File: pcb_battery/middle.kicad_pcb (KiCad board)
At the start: 2 copper layers, 100 x 29.9 mm, 8 parts, among them J1 BAT+, J2 BAT-, J3 TOP+, J4 BOT+, J5 TOP-, J6 BOT-

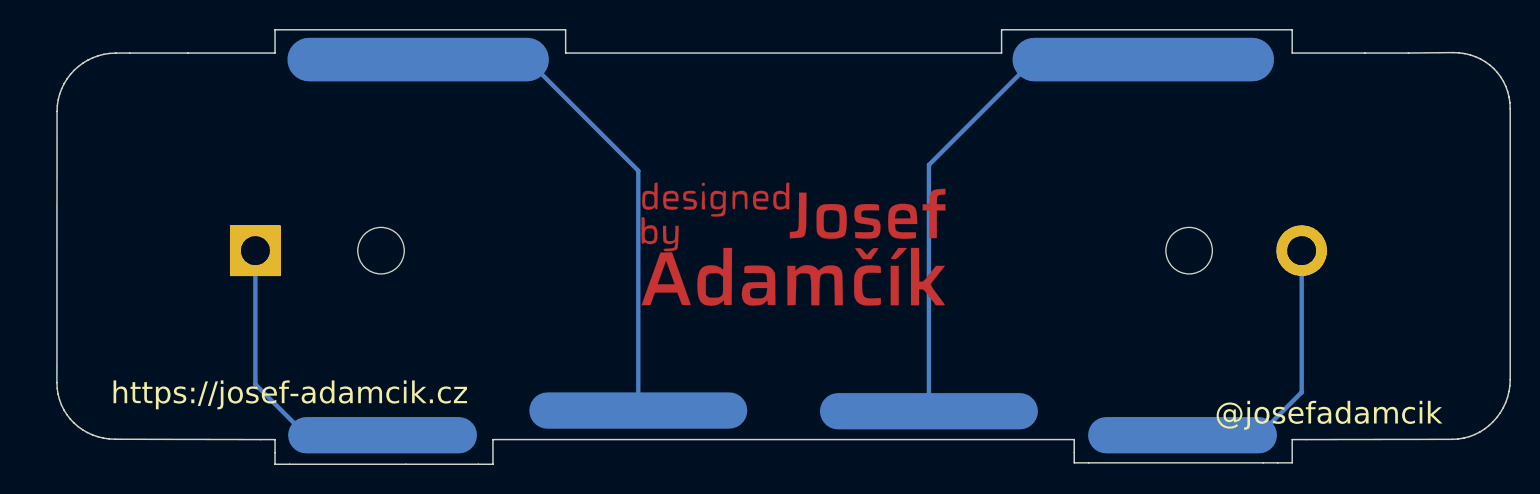
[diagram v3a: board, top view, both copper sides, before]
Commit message: Update trace and via sizes for battery and charger
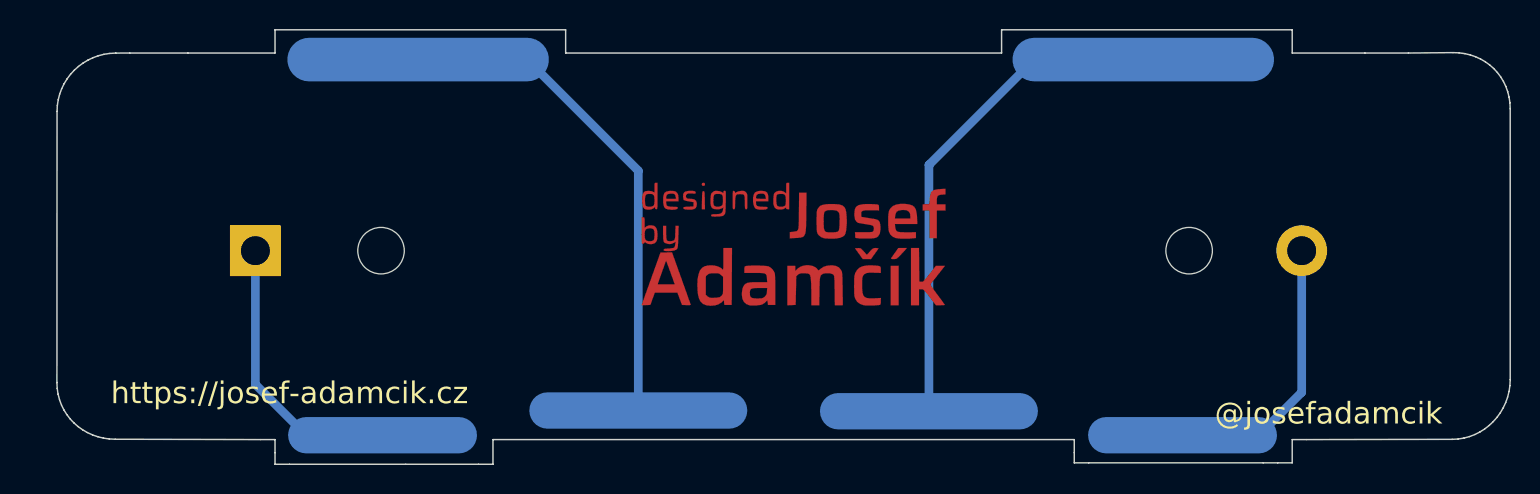
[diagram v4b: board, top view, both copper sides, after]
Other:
- net class Battery added: clearance 0.4, trace_width 0.6, via_dia 1.2, via_drill 1
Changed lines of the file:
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@@
-(kicad_pcb (version 20171130) (host pcbnew 5.1.4-e60b266~84~ubuntu19.04.1)
+(kicad_pcb (version 20171130) (host pcbnew 5.1.5-52549c5~84~ubuntu19.04.1)
   (general
     (thickness 1.6)
@@
     (via_dia 0.6)
     (via_drill 0.4)
+    (uvia_dia 0.3)
+    (uvia_drill 0.1)
+  )
+  (net_class Battery ""
+    (clearance 0.4)
+    (trace_width 0.6)
+    (via_dia 1.2)
+    (via_drill 1)
     (uvia_dia 0.3)
     (uvia_drill 0.1)
@@
   (gr_line (start -45.966545 -42.995933) (end -45.966593 -42.99593) (layer Edge.Cuts) (width 0.1))
   (gr_line (start -45.966593 -42.99593) (end -45.966593 -42.99593) (layer Edge.Cuts) (width 0.1))
-  (segment (start -32.85 -16.7) (end -27.6 -16.7) (width 0.3) (layer B.Cu) (net 1))
-  (segment (start -36.35 -20.2) (end -32.85 -16.7) (width 0.3) (layer B.Cu) (net 1))
-  (segment (start -36.35 -29.4) (end -36.35 -20.2) (width 0.3) (layer B.Cu) (net 1))
-  (segment (start 32.7 -16.7) (end 27.45 -16.7) (width 0.3) (layer B.Cu) (net 2))
-  (segment (start 35.65 -19.65) (end 32.7 -16.7) (width 0.3) (layer B.Cu) (net 2))
-  (segment (start 35.65 -29.4) (end 35.65 -19.65) (width 0.3) (layer B.Cu) (net 2))
-  (segment (start -17.65 -42.55) (end -25.15 -42.55) (width 0.3) (layer B.Cu) (net 3))
-  (segment (start -10 -34.9) (end -17.65 -42.55) (width 0.3) (layer B.Cu) (net 3))
-  (segment (start -10 -18.4) (end -10 -34.9) (width 0.3) (layer B.Cu) (net 3))
-  (segment (start 17.25 -42.55) (end 24.75 -42.55) (width 0.3) (layer B.Cu) (net 4))
-  (segment (start 10 -35.3) (end 17.25 -42.55) (width 0.3) (layer B.Cu) (net 4))
-  (segment (start 10 -18.35) (end 10 -35.3) (width 0.3) (layer B.Cu) (net 4))
+  (segment (start -32.85 -16.7) (end -27.6 -16.7) (width 0.6) (layer B.Cu) (net 1))
+  (segment (start -36.35 -20.2) (end -32.85 -16.7) (width 0.6) (layer B.Cu) (net 1))
+  (segment (start -36.35 -29.4) (end -36.35 -20.2) (width 0.6) (layer B.Cu) (net 1))
+  (segment (start 32.7 -16.7) (end 27.45 -16.7) (width 0.6) (layer B.Cu) (net 2))
+  (segment (start 35.65 -19.65) (end 32.7 -16.7) (width 0.6) (layer B.Cu) (net 2))
+  (segment (start 35.65 -29.4) (end 35.65 -19.65) (width 0.6) (layer B.Cu) (net 2))
+  (segment (start -17.65 -42.55) (end -25.15 -42.55) (width 0.6) (layer B.Cu) (net 3))
+  (segment (start -10 -34.9) (end -17.65 -42.55) (width 0.6) (layer B.Cu) (net 3))
+  (segment (start -10 -18.4) (end -10 -34.9) (width 0.6) (layer B.Cu) (net 3))
+  (segment (start 17.25 -42.55) (end 24.75 -42.55) (width 0.6) (layer B.Cu) (net 4))
+  (segment (start 10 -35.3) (end 17.25 -42.55) (width 0.6) (layer B.Cu) (net 4))
+  (segment (start 10 -18.35) (end 10 -35.3) (width 0.6) (layer B.Cu) (net 4))
 )
